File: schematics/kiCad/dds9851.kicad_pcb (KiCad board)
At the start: 2 copper layers, 59 x 53 mm, 12 parts, among them M3 MountingHole_3.2mm_M3, U1 Teensy-LC, U2 HC06

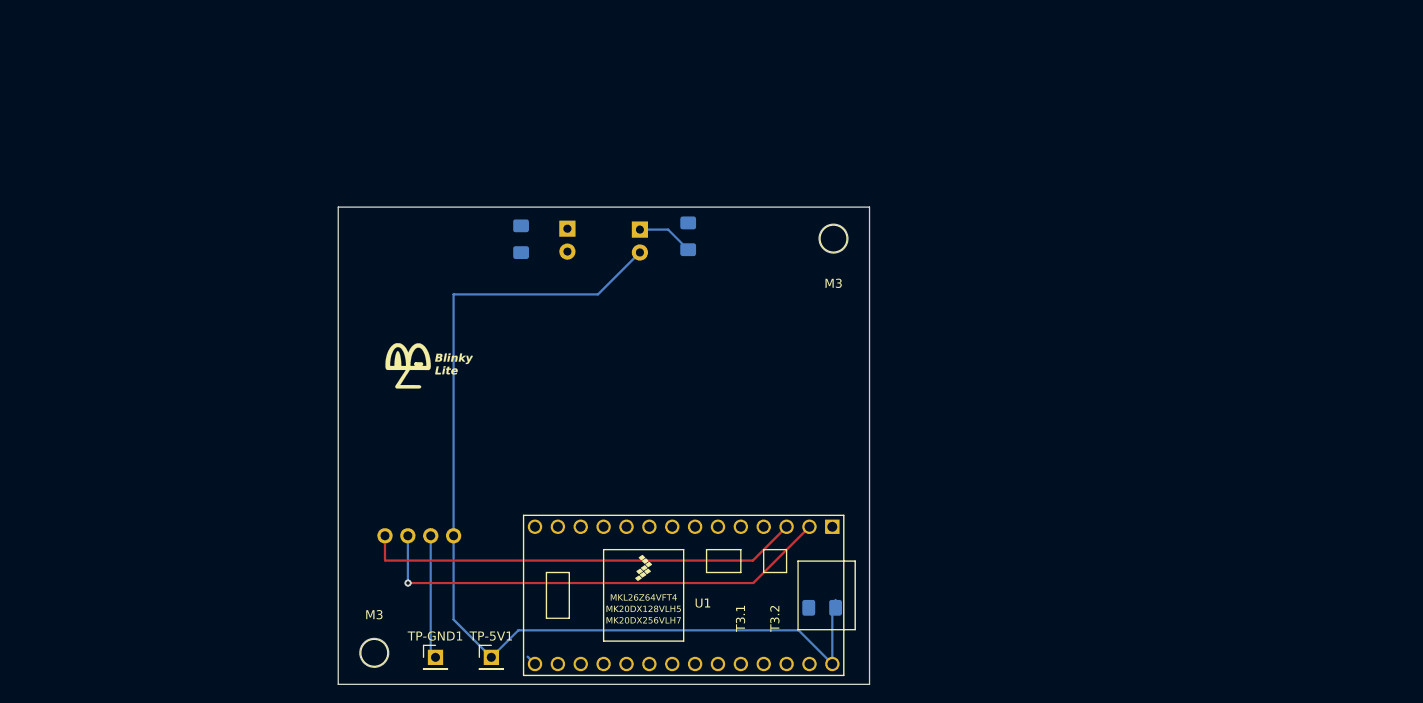
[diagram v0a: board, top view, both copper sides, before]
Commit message: schematic done - working on pcb
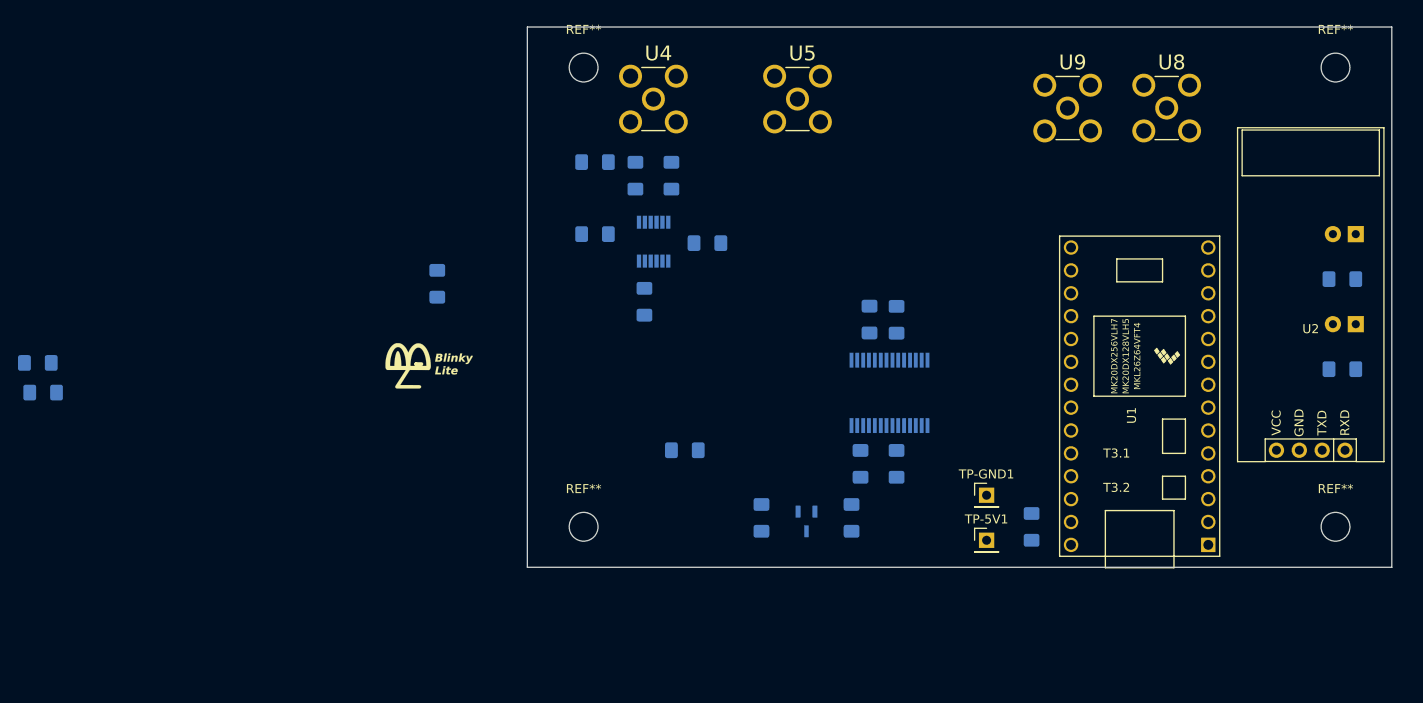
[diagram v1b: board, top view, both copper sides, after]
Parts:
- removed M3 (x2): MountingHole_3.2mm_M3, MountingHole:MountingHole_3.2mm_M3
- added C10: 0.1 uF, Capacitor_SMD:C_1206_3216Metric_Pad1.42x1.75mm_HandSolder, B.Cu at (169.0, 98.5)
- added C11: 0.1 uF, Capacitor_SMD:C_1206_3216Metric_Pad1.42x1.75mm_HandSolder, B.Cu at (170.0, 82.5)
- added C2: 1 uF, Capacitor_SMD:C_1206_3216Metric_Pad1.42x1.75mm_HandSolder, B.Cu at (158.0, 104.5)
- added C3: 1 uF, Capacitor_SMD:C_1206_3216Metric_Pad1.42x1.75mm_HandSolder, B.Cu at (168.0, 104.5)
- added C4: 10 nF, Capacitor_SMD:C_1206_3216Metric_Pad1.42x1.75mm_HandSolder, B.Cu at (144.0, 66.5)
- added C5: 10 nF, Capacitor_SMD:C_1206_3216Metric_Pad1.42x1.75mm_HandSolder, B.Cu at (148.0, 66.5)
- added C6: 0.1 uF, Capacitor_SMD:C_1206_3216Metric_Pad1.42x1.75mm_HandSolder, B.Cu at (139.5, 73.0)
- added C7: 0.1 uF, Capacitor_SMD:C_1206_3216Metric_Pad1.42x1.75mm_HandSolder, B.Cu at (145.0, 80.5)
- added C8: 0.1 uF, Capacitor_SMD:C_1206_3216Metric_Pad1.42x1.75mm_HandSolder, B.Cu at (173.0, 98.5)
- added C9: 0.1 uF, Capacitor_SMD:C_1206_3216Metric_Pad1.42x1.75mm_HandSolder, B.Cu at (173.0, 82.5)
- added R3: 50, Resistor_SMD:R_1206_3216Metric_Pad1.42x1.75mm_HandSolder, B.Cu at (139.5, 65.0)
- added R4: 450, Resistor_SMD:R_1206_3216Metric_Pad1.42x1.75mm_HandSolder, B.Cu at (152.0, 74.0)
- added R5: 1k, Resistor_SMD:R_1206_3216Metric_Pad1.42x1.75mm_HandSolder, B.Cu at (149.5, 97.0)
- added R6: 3.9k, Resistor_SMD:R_1206_3216Metric_Pad1.42x1.75mm_HandSolder, B.Cu at (122.0, 78.5)
- added R7: 51, Resistor_SMD:R_1206_3216Metric_Pad1.42x1.75mm_HandSolder, B.Cu at (77.6, 87.3)
- added R8: 51, Resistor_SMD:R_1206_3216Metric_Pad1.42x1.75mm_HandSolder, B.Cu at (78.2, 90.6)
- added REF**: MountingHole_3.2mm_M3, MountingHole:MountingHole_3.2mm_M3, F.Cu at (138.2, 105.5)
- added REF**: MountingHole_3.2mm_M3, MountingHole:MountingHole_3.2mm_M3, F.Cu at (138.2, 54.5)
- added REF**: MountingHole_3.2mm_M3, MountingHole:MountingHole_3.2mm_M3, F.Cu at (221.8, 105.5)
- added REF**: MountingHole_3.2mm_M3, MountingHole:MountingHole_3.2mm_M3, F.Cu at (221.8, 54.5)
- added U3: MCP1700T-3302E_TT, MCP1700T:SOT95P237X112-3N, B.Cu at (163.0, 104.9)
- added U4: 901-144, SMA_Female:SMA_Female, F.Cu at (146.0, 58.0)
- added U5: 901-144, SMA_Female:SMA_Female, F.Cu at (162.0, 58.0)
- added U6: LTC6957HMS-4#PBF, LTC6957:SOP65P490X110-12N, B.Cu at (146.0, 73.8)
- added U7: AD9851BRSZ, AD9851:SOP65P780X200-28N, B.Cu at (172.2, 90.6)
- added U8: 901-144, SMA_Female:SMA_Female, F.Cu at (203.0, 59.0)
- added U9: 901-144, SMA_Female:SMA_Female, F.Cu at (192.0, 59.0)
- U2: moved to F.Cu
- moved U2 99.5 mm to (219.0, 97.0), turned to 180 degrees
- moved R2 91.3 mm to (222.5, 78.0), turned to 0 degrees
- moved D2 87.6 mm to (224.0, 73.0), turned to 180 degrees
- moved D1 80.2 mm to (224.0, 83.0), turned to 180 degrees
- moved R1 74.1 mm to (222.5, 88.0), turned to 0 degrees
- moved TP-GND1 63.8 mm to (183.0, 102.0)
- moved TP-5V1 56.5 mm to (183.0, 107.0)
- moved U1 55.3 mm to (200.0, 91.0), turned to 90 degrees
- moved C1 24.9 mm to (188.0, 105.5), turned to 270 degrees
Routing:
- net +5V: track 112.9 -> 0.00 mm
- net Net-(U1-Pad2): track 52.4 -> 0.00 mm, vias 1 -> 0
- net Net-(U1-Pad3): track 48.9 -> 0.00 mm
- net GND: track 13.7 -> 0.00 mm
- net Net-(D1-Pad1): track 6.28 -> 0.00 mm
- net Net-(D2-Pad2): track 1.14 -> 0.00 mm
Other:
- board size 59 x 53 mm -> 96 x 60 mm

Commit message: components placed
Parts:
- removed the C1 at (188.0, 105.5)
- removed C11, C9: 0.1 uF, Capacitor_SMD:C_1206_3216Metric_Pad1.42x1.75mm_HandSolder
- removed the C8 at (173.0, 98.5)
- moved R8 106.4 mm to (184.5, 96.5), turned to 180 degrees
- moved R7 97.3 mm to (174.5, 96.5)
- moved C3 65.1 mm to (206.0, 60.5)
- moved R6 58.5 mm to (179.9, 70.4), turned to 0 degrees
- moved U6 58.1 mm to (201.0, 60.9)
- moved C5 57.6 mm to (200.5, 57.0), turned to 180 degrees
- moved U8 54.9 mm to (173.0, 105.0)
- moved U1 47.3 mm to (151.0, 105.0)
- moved U3 47.0 mm to (162.0, 105.0)
- moved U9 46.7 mm to (184.0, 105.0)
- moved TP-5V1 41.8 mm to (202.5, 70.0)
- moved C6 40.5 mm to (179.9, 76.6), turned to 180 degrees
- moved TP-GND1 34.7 mm to (196.5, 70.0)
- moved G*** 30.1 mm to (144.6, 68.6)
- moved R5 29.7 mm to (162.7, 70.4)
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- renumbered C4 to C1, C5 to C2, C2 to C3, C7 to C4, C3 to C5, C10 to C8, D2 to D1, D1 to D2, R3 to R1, R1 to R3, U4 to U1, U5 to U3, U6 to U4, U1 to U5, U3 to U6
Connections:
- U4 pad 10: Net-(U6-Pad10) -> Net-(R4-Pad1)
- U4 pad 9: Net-(R4-Pad1) -> Net-(U4-Pad9)
- U7 pad 9: Net-(U6-Pad10) -> Net-(U4-Pad9)

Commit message: update
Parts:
- moved U4 13.9 mm to (155.8, 76.9)
- moved C4 12.4 mm to (155.8, 84.1)
- moved C2 12.1 mm to (149.0, 74.9), turned to 90 degrees
- moved C8 12.0 mm to (162.5, 64.6)
- moved C1 10.4 mm to (149.0, 80.7), turned to 270 degrees
- moved R1 9.07 mm to (143.1, 82.0)
- moved C6 0.60 mm to (180.5, 76.6)
- moved R4 0.49 mm to (162.0, 96.0)
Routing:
- net Net-(C1-Pad2): track 0.00 -> 28.1 mm
- net Net-(R7-Pad1): track 0.00 -> 25.8 mm
- net Net-(R4-Pad1): track 0.00 -> 19.5 mm
- net Net-(U4-Pad9): track 0.00 -> 16.3 mm
- net Net-(R8-Pad2): track 0.00 -> 8.91 mm
- net +3V3: track 0.00 -> 8.85 mm
- net Net-(R4-Pad2): track 0.00 -> 7.51 mm
- net Net-(C1-Pad1): track 0.00 -> 5.45 mm
- net Net-(C2-Pad1): track 0.00 -> 4.72 mm

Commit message: pcb ready
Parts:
- removed G***: LOGO, blinkyLiteLogo:blinkyLiteLogo
- removed U1, U3, U8, U9: 901-144, SMA_Female:SMA_Female
- added J1: 2985-6004, 2985-6004:AMPHENOL_2985-6004, F.Cu at (144.5, 94.5)
- added J2: 2985-6004, 2985-6004:AMPHENOL_2985-6004, F.Cu at (155.5, 94.5)
- added J3: 2985-6004, 2985-6004:AMPHENOL_2985-6004, F.Cu at (171.0, 94.5)
- added J4: 2985-6004, 2985-6004:AMPHENOL_2985-6004, F.Cu at (182.0, 94.5)
- moved R4 12.2 mm to (160.0, 84.0)
- moved R7 9.71 mm to (172.5, 87.0)
- moved R8 9.55 mm to (183.5, 87.0)
- moved R5 4.47 mm to (166.5, 68.0), turned to 0 degrees
- moved C8 4.12 mm to (166.5, 63.5)
- moved R6 0.62 mm to (180.5, 70.4)
- renumbered REF** to REF1, REF** to REF2, REF** to REF3, REF** to REF4
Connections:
- U7 pad 22: Net-(U5-Pad28) -> Net-(U5-Pad29)
- U7 pad 8: Net-(U5-Pad29) -> Net-(U5-Pad28)
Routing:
- net +3V3: track 8.85 -> 125.5 mm
- net +5V: track 0.00 -> 81.7 mm
- net Net-(U5-Pad28): track 0.00 -> 54.9 mm, vias 0 -> 1
- net Net-(U5-Pad27): track 0.00 -> 54.7 mm, vias 0 -> 1
- net Net-(U5-Pad30): track 0.00 -> 54.3 mm, vias 0 -> 1
- net Net-(U5-Pad29): track 0.00 -> 51.1 mm, vias 0 -> 1
- net GND: track 0.00 -> 34.8 mm, vias 0 -> 39
- net Net-(D1-Pad2): track 0.00 -> 30.1 mm
- net Net-(U2-Pad1): track 0.00 -> 17.4 mm
- net Net-(U2-Pad2): track 0.00 -> 16.0 mm
- net Net-(J4-Pad1): track 8.91 -> 21.8 mm
- net Net-(R4-Pad1): track 19.5 -> 6.69 mm
- net Net-(J3-Pad1): track 25.8 -> 14.5 mm
- net Net-(C1-Pad2): track 28.1 -> 17.0 mm
- net Net-(R5-Pad1): track 0.00 -> 7.27 mm
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- added copper zone on B.Cu, net GND
- added copper zone on F.Cu, net GND
